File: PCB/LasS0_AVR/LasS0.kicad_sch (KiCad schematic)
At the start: 42 parts, among them J1 CiKe2PinSock, J1_1 CiKe2PinPlug, J2 CiKe2PinSock, J2_1 CiKe2PinPlug, J3 CiKe2PinSock, J3_1 CiKe2PinPlug, J4 CiKe2PinSock, J4_1 CiKe2PinPlug, Q2 AO3400A, U1 TPS54331D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

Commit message: Update AVR schematic for initial test
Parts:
- removed C?: C_Small, symbol Device:C_Small
- added C?: 22pF, symbol Device:C_Small
- added J? (x5): Conn_01x01, symbol Connector_Generic:Conn_01x01
- added JP1_VCC: S0+ VCC, Jumper:SolderJumper-2_P1.3mm_Open_TrianglePad1.0x1.5mm, symbol Jumper:SolderJumper_2_Open
- added JP2_D: DO PD, Jumper:SolderJumper-2_P1.3mm_Open_TrianglePad1.0x1.5mm, symbol Jumper:SolderJumper_2_Open
- added R?: 10k, Resistor_SMD:R_0603_1608Metric, symbol Device:R
- C?: value C_Small -> 22pF
- Y?: value Crystal -> 8 MHz
- renumbered JP2_D2 to JP1_D, JP2_U2 to JP1_PU
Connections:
- net +5V: now also J?.1 (Pin_1)
- net D0: now also JP2_D.1 (A)
- net GND: now also C?.1, J?.1 (Pin_1), R?.2
- net S0+: now also JP1_VCC.2 (B)
- net VCC: now also JP1_VCC.1 (A)
- net at U?.2 (XTAL1/PB0), Y?.2: now also C?.2
- net at U?.10 (PA3): now also J?.1 (Pin_1)
- net at U?.12 (PA1): now also J?.1 (Pin_1)
- net at U?.6 (PA7): now also J?.1 (Pin_1)
- new net: JP2_D.2 (B), R?.1
- no-connect marks 12 -> 9
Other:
- note added: "Output configuration SO+ PU and SO- GND set: Pulled up inverted output SO+ VCC alone set: VCC output on SO- like pushbutton"
- note removed: "Enable both for pulled-up switching keep disabled for open collector S0 out"
- moved on the sheet: C?, D3, H1, H2, J2, J2_1, J?, JP1_D, JP1_PU, LOGO1, LOGO3, Q2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

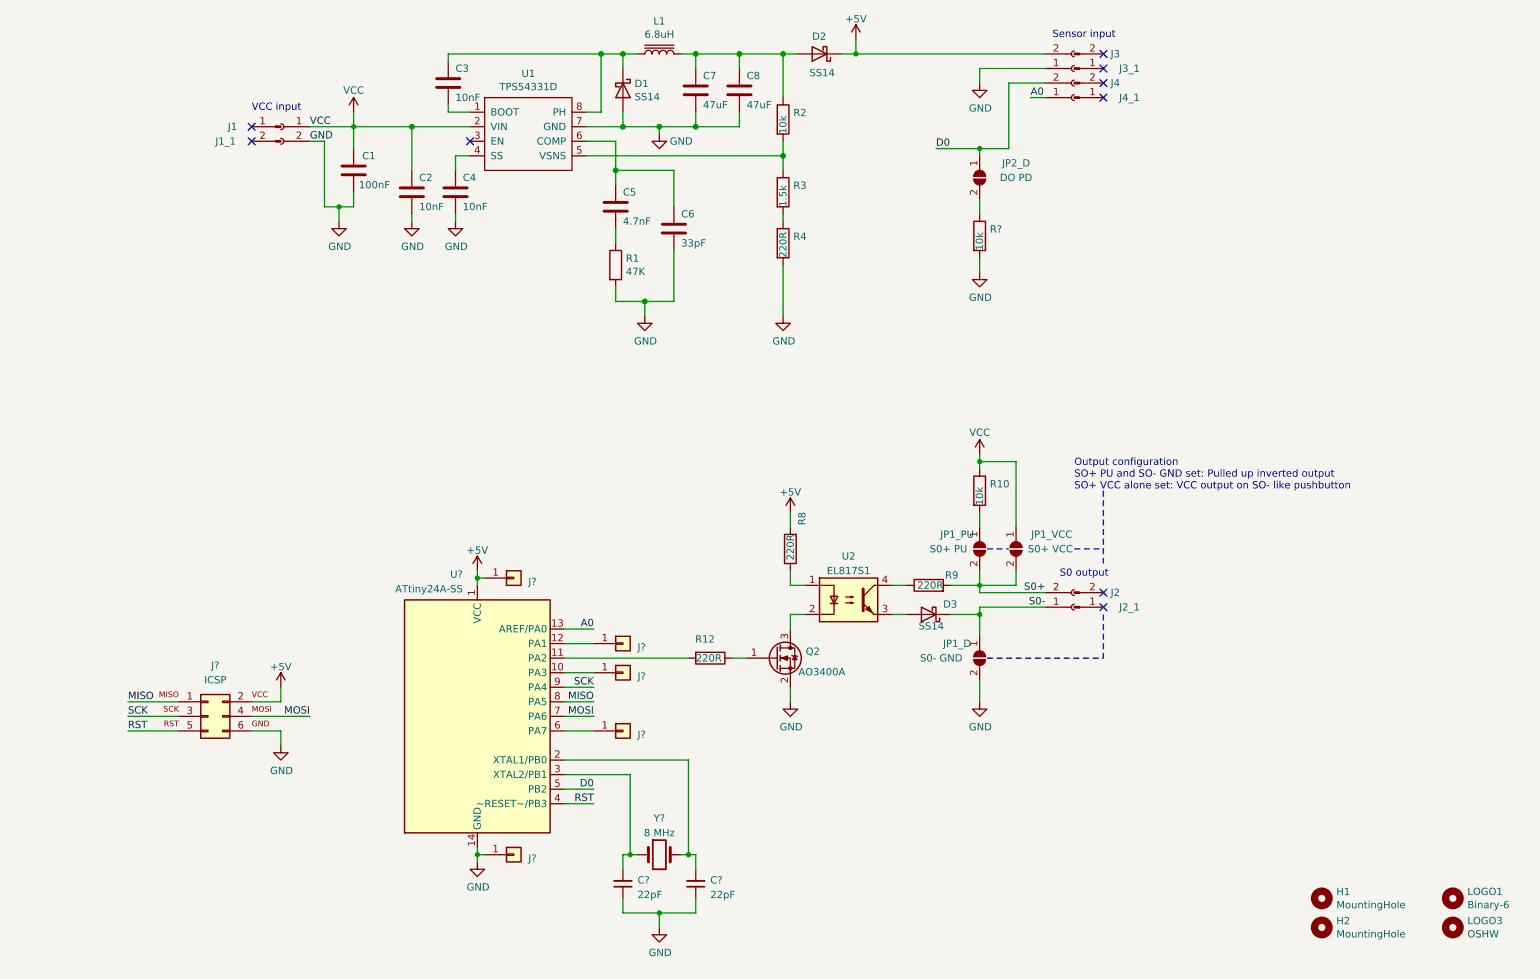
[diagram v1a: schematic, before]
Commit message: [Schematic] Update component fields and add decoupling cap
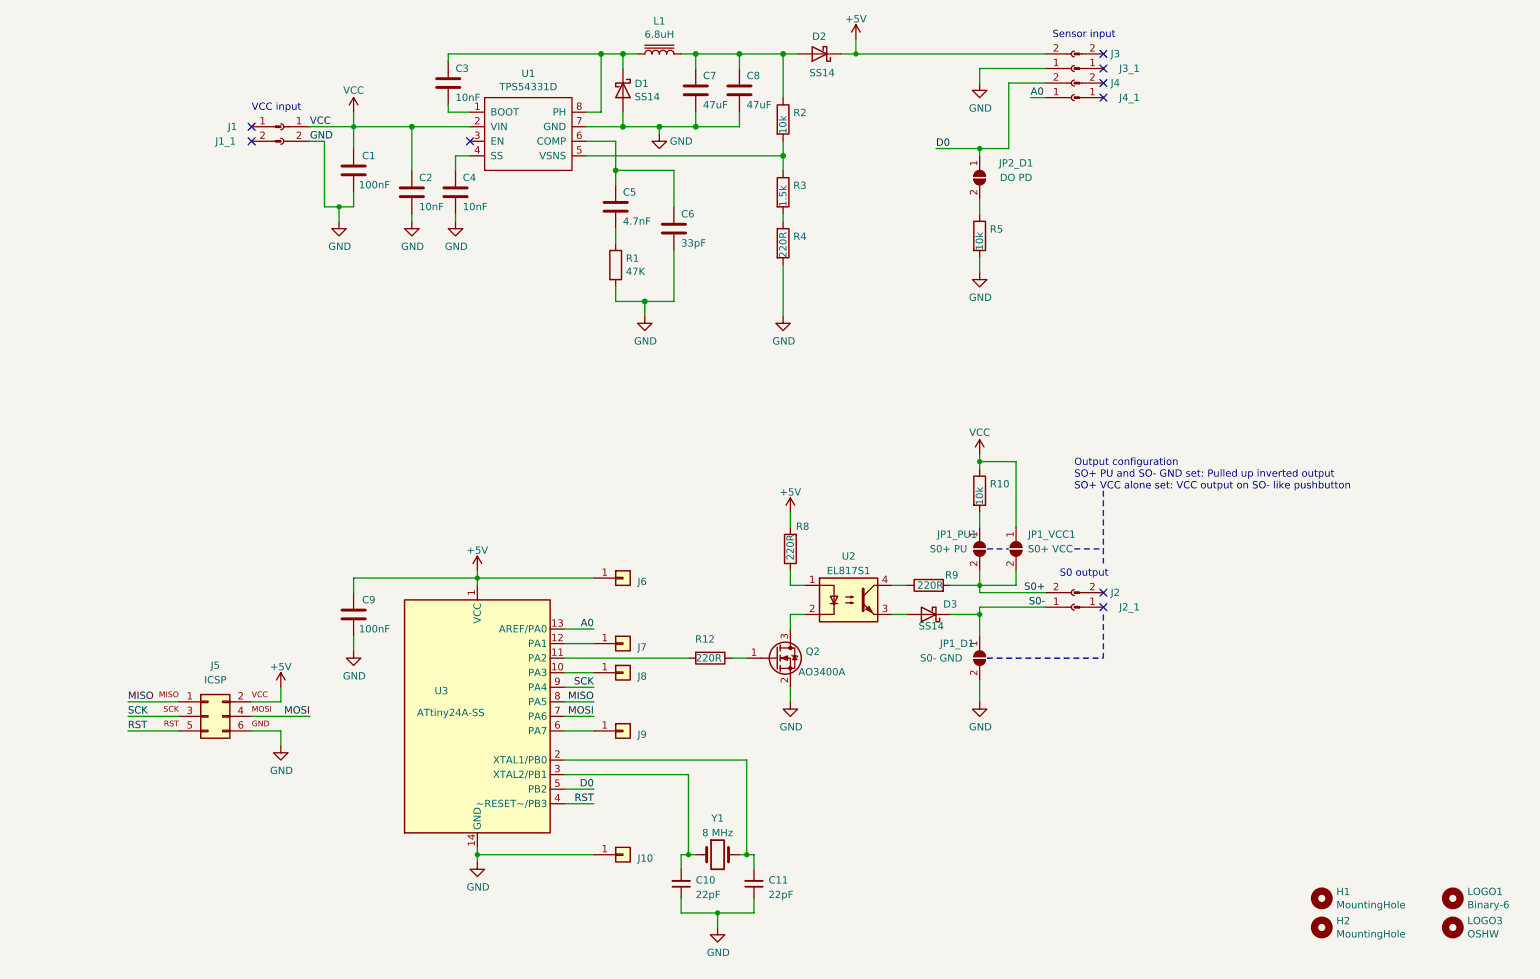
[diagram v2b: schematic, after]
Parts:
- added C9: 100nF, Capacitor_SMD:C_0603_1608Metric, symbol Device:C
- C10, C11: renamed from C?; footprint (none) -> Capacitor_SMD:C_0603_1608Metric; LCSC (none) -> C1653
- J10, J6, J7, J8, J9: renamed from J?; footprint (none) -> MeineModule:PinheaderOwn
- J5: renamed from J?; footprint (none) -> MeineBib:AVR_ISP
- U3: renamed from U?; LCSC (none) -> C14909
- Y1: renamed from Y?; footprint (none) -> Crystal:Crystal_SMD_5032-2Pin_5.0x3.2mm; LCSC (none) -> C115962
- gave numbers to parts that had none: 1
- renumbered JP1_D to JP1_D1, JP1_PU to JP1_PU1, JP1_VCC to JP1_VCC1, JP2_D to JP2_D1
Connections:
- net +5V: now also C9.2
- net GND: now also C9.1
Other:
- moved on the sheet: C10, C11, J10, J6, Y1

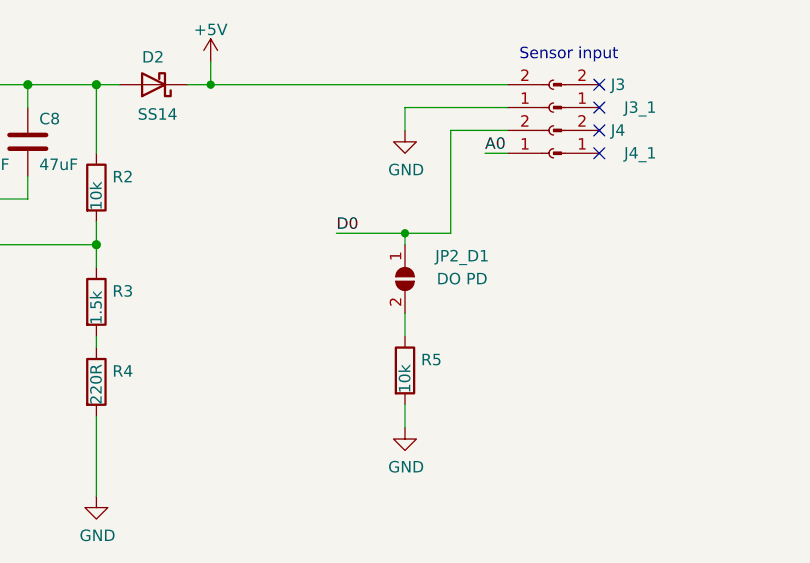
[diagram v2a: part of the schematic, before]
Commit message: [PCB] Implement AVR on PCB
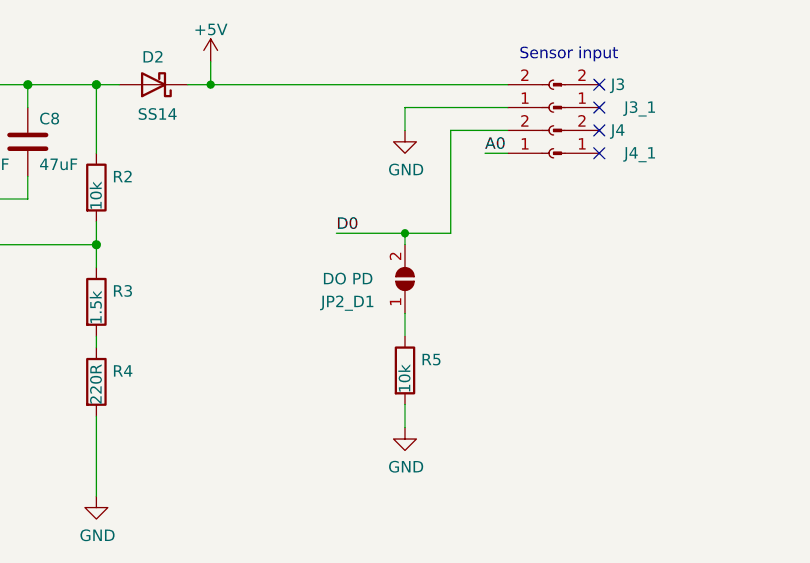
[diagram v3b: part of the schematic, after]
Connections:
- net D0: now also JP2_D1.2 (B); no longer JP2_D1.1 (A)
- net at R5.1: now also JP2_D1.1 (A); no longer JP2_D1.2 (B)
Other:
- moved on the sheet: JP2_D1
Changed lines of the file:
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@@
     (pin "2")
   )
-  (symbol (lib_id "Jumper:SolderJumper_2_Open") (at 189.23 45.72 90) (mirror x) (unit 1)
+  (symbol (lib_id "Jumper:SolderJumper_2_Open") (at 189.23 45.72 270) (mirror x) (unit 1)
     (in_bom no) (on_board yes)
-    (property "Reference" "JP2_D1" (id 0) (at 195.58 43.18 90))
-    (property "Value" "DO PD" (id 1) (at 195.58 45.72 90))
+    (property "Reference" "JP2_D1" (id 0) (at 182.88 48.26 90))
+    (property "Value" "DO PD" (id 1) (at 182.88 45.72 90))
     (property "Footprint" "Jumper:SolderJumper-2_P1.3mm_Open_TrianglePad1.0x1.5mm" (id 2) (at 189.23 45.72 0)
       (effects (font (size 1.27 1.27)) hide)
